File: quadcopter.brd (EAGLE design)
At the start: 137.2 x 137.2 mm, 66 parts, among them J4 AVR_SPI_PRG_6NS, U2 ATMEGA128RFA1

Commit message: CompilingGerber
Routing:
- net VBAT: track 310.7 -> 311.9 mm
- net GND: track 337.0 -> 337.8 mm
- net PE3: track 86.5 -> 87.2 mm
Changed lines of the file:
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@@
 <layer number="13" name="Route13" color="4" fill="5" visible="no" active="no"/>
 <layer number="14" name="Route14" color="1" fill="6" visible="no" active="no"/>
-<layer number="15" name="Route15" color="4" fill="6" visible="no" active="yes"/>
+<layer number="15" name="Route15" color="4" fill="6" visible="yes" active="yes"/>
 <layer number="16" name="Bottom" color="1" fill="1" visible="yes" active="yes"/>
 <layer number="17" name="Pads" color="2" fill="1" visible="yes" active="yes"/>
@@
 <layer number="25" name="tNames" color="7" fill="1" visible="yes" active="yes"/>
 <layer number="26" name="bNames" color="7" fill="1" visible="yes" active="yes"/>
-<layer number="27" name="tValues" color="7" fill="1" visible="yes" active="yes"/>
+<layer number="27" name="tValues" color="7" fill="1" visible="no" active="yes"/>
 <layer number="28" name="bValues" color="7" fill="1" visible="yes" active="yes"/>
-<layer number="29" name="tStop" color="7" fill="3" visible="no" active="yes"/>
+<layer number="29" name="tStop" color="7" fill="3" visible="yes" active="yes"/>
 <layer number="30" name="bStop" color="7" fill="6" visible="no" active="yes"/>
 <layer number="31" name="tCream" color="7" fill="4" visible="no" active="yes"/>
@@
 <layer number="49" name="Reference" color="7" fill="1" visible="yes" active="yes"/>
 <layer number="50" name="dxf" color="7" fill="1" visible="no" active="no"/>
-<layer number="51" name="tDocu" color="7" fill="1" visible="yes" active="yes"/>
+<layer number="51" name="tDocu" color="7" fill="1" visible="no" active="yes"/>
 <layer number="52" name="bDocu" color="7" fill="1" visible="yes" active="yes"/>
 <layer number="53" name="tGND_GNDA" color="7" fill="9" visible="no" active="no"/>
@@
 <wire x1="-28.6385" y1="-38.9255" x2="-38.354" y2="-38.9255" width="0.1524" layer="42"/>
 <wire x1="-38.354" y1="-38.9255" x2="-38.354" y2="-24.7015" width="0.1524" layer="42"/>
+<dimension x1="-5.08" y1="68.58" x2="-5.08" y2="-68.58" x3="-73.4695" y3="0" textsize="1.778" layer="48" unit="inch"/>
 </plain>
 <attributes>
@@
 <wire x1="1.9812" y1="-26.4414" x2="1.96" y2="-26.4355" width="0.1524" layer="1"/>
 <wire x1="-0.1524" y1="-27.432" x2="1.905" y2="-27.432" width="0.1524" layer="1"/>
-<wire x1="-1.3716" y1="-26.2128" x2="-0.1524" y2="-27.432" width="0.1524" layer="1"/>
-<wire x1="-1.9812" y1="-26.2128" x2="-1.3716" y2="-26.2128" width="0.1524" layer="1"/>
-<wire x1="-3.2766" y1="-27.5082" x2="-1.9812" y2="-26.2128" width="0.1524" layer="1"/>
+<wire x1="-1.3716" y1="-26.0223" x2="-0.1524" y2="-27.432" width="0.1524" layer="1"/>
+<wire x1="-1.9812" y1="-26.0223" x2="-1.3716" y2="-26.0223" width="0.1524" layer="1"/>
+<wire x1="-3.2766" y1="-27.5082" x2="-1.9812" y2="-26.0223" width="0.1524" layer="1"/>
 <wire x1="1.905" y1="-27.432" x2="1.96" y2="-27.4355" width="0.1524" layer="1"/>
 <wire x1="-3.2766" y1="-27.5082" x2="-3.302" y2="-27.559" width="0.1524" layer="1"/>
-<wire x1="-9.0678" y1="-31.4706" x2="-10.4394" y2="-32.8422" width="0" layer="19" extent="1-16"/>
 <wire x1="-20.8026" y1="-32.8422" x2="-20.828" y2="-32.899" width="0.1524" layer="1"/>
 <wire x1="-9.0678" y1="-31.4706" x2="-9.023" y2="-31.4325" width="0.1524" layer="1"/>
@@
 <wire x1="-7.6962" y1="-24.4602" x2="-7.802" y2="-24.4355" width="0.1524" layer="1"/>
 <wire x1="-6.7818" y1="-22.7838" x2="-6.8199" y2="-22.7457" width="0.1524" layer="1"/>
-<wire x1="-5.1054" y1="-20.3454" x2="-2.5146" y2="-20.3454" width="0.1524" layer="16"/>
-<wire x1="-5.1816" y1="-20.3454" x2="-5.1054" y2="-20.3454" width="0.1524" layer="1"/>
+<wire x1="-4.1529" y1="-21.1709" x2="-2.5146" y2="-20.3454" width="0.1524" layer="16"/>
+<wire x1="-5.1816" y1="-20.3454" x2="-4.1529" y2="-21.1709" width="0.1524" layer="1"/>
 <wire x1="18.5166" y1="23.0886" x2="19.3548" y2="23.0886" width="0.1524" layer="1"/>
 <wire x1="1.4478" y1="6.0198" x2="18.5166" y2="23.0886" width="0.1524" layer="1"/>
@@
 <via x="-0.9144" y="-21.1074" extent="1-16" drill="0.381"/>
 <via x="-2.5146" y="-20.3454" extent="1-16" drill="0.381"/>
-<via x="-5.1054" y="-20.3454" extent="1-16" drill="0.381"/>
+<via x="-4.1529" y="-21.1709" extent="1-16" drill="0.381"/>
 <via x="-4.6482" y="8.382" extent="1-16" drill="0.381"/>
 <via x="-21.209" y="-25.7175" extent="1-16" drill="0.6"/>
@@
 <wire x1="2.2098" y1="-38.9382" x2="2.2098" y2="-43.1292" width="0.1524" layer="1"/>
 <wire x1="2.2098" y1="-19.5072" x2="2.2098" y2="-38.9382" width="0.1524" layer="16"/>
-<wire x1="1.7526" y1="-19.05" x2="2.2098" y2="-19.5072" width="0.1524" layer="16"/>
-<wire x1="1.0668" y1="-19.05" x2="1.7526" y2="-19.05" width="0.1524" layer="1"/>
+<wire x1="2.3241" y1="-18.542" x2="2.2098" y2="-19.5072" width="0.1524" layer="16"/>
+<wire x1="1.0668" y1="-19.05" x2="2.3241" y2="-18.542" width="0.1524" layer="1"/>
 <wire x1="0.8382" y1="-18.8214" x2="1.0668" y2="-19.05" width="0.1524" layer="1"/>
 <wire x1="2.2098" y1="-43.1292" x2="2.2225" y2="-43.1775" width="0.1524" layer="1"/>
@@
 <wire x1="0.9144" y1="-16.4592" x2="0.2286" y2="-16.4592" width="0.1524" layer="16"/>
 <wire x1="1.7526" y1="-17.2974" x2="0.9144" y2="-16.4592" width="0.1524" layer="16"/>
-<wire x1="1.7526" y1="-19.05" x2="1.7526" y2="-17.2974" width="0.1524" layer="16"/>
+<wire x1="2.3241" y1="-18.542" x2="1.7526" y2="-17.2974" width="0.1524" layer="16"/>
 <via x="2.2098" y="-38.9382" extent="1-16" drill="0.381"/>
-<via x="1.7526" y="-19.05" extent="1-16" drill="0.381"/>
+<via x="2.3241" y="-18.542" extent="1-16" drill="0.381"/>
 </signal>
 <signal name="PE2">
@@
 <wire x1="-5.715" y1="-0.3051" x2="-5.715" y2="-1.5265" width="0.1524" layer="1"/>
 <wire x1="-2.1336" y1="-27.5082" x2="-2.1336" y2="-28.4988" width="0.1524" layer="1"/>
-<wire x1="-1.6764" y1="-27.051" x2="-2.1336" y2="-27.5082" width="0.1524" layer="1"/>
-<wire x1="-1.6764" y1="-24.9174" x2="-1.6764" y2="-27.051" width="0.1524" layer="16"/>
+<wire x1="-1.6764" y1="-26.924" x2="-2.1336" y2="-27.5082" width="0.1524" layer="1"/>
+<wire x1="-1.6764" y1="-24.9174" x2="-1.6764" y2="-26.924" width="0.1524" layer="16"/>
 <wire x1="-7.62" y1="-18.9738" x2="-1.6764" y2="-24.9174" width="0.1524" layer="16"/>
 <wire x1="-7.62" y1="-4.3434" x2="-7.62" y2="-18.9738" width="0.1524" layer="16"/>
@@
 <wire x1="-34.29" y1="13.9446" x2="-34.29" y2="13.97" width="0.1524" layer="16"/>
 <wire x1="-7.62" y1="-4.3434" x2="-7.62" y2="-4.191" width="0.1524" layer="16"/>
-<via x="-1.6764" y="-27.051" extent="1-16" drill="0.381"/>
+<via x="-1.6764" y="-26.924" extent="1-16" drill="0.381"/>
 <via x="-7.62" y="-4.191" extent="1-16" drill="0.381"/>
 </signal>
@@
 <wire x1="-5.715" y1="1.0721" x2="-5.715" y2="1.9025" width="0.1524" layer="1"/>
 <wire x1="-2.7432" y1="-30.2514" x2="-2.7432" y2="-28.575" width="0.1524" layer="1"/>
-<wire x1="-6.1722" y1="-33.6804" x2="-3.946525" y2="-31.454725" width="0" layer="19" extent="1-16"/>
 <wire x1="-3.946525" y1="-31.454725" x2="-2.7432" y2="-30.2514" width="0.1524" layer="1"/>
 <wire x1="-33.4518" y1="10.5918" x2="-33.4518" y2="1.905" width="0.1524" layer="1"/>
@@
 <wire x1="4.4958" y1="-38.7858" x2="4.4958" y2="-36.957" width="0.4572" layer="16"/>
 <wire x1="3.2004" y1="-40.0812" x2="4.4958" y2="-38.7858" width="0.4572" layer="16"/>
-<wire x1="3.2004" y1="-47.1678" x2="3.2004" y2="-40.0812" width="0.4572" layer="16"/>
-<wire x1="2.3622" y1="-48.006" x2="3.2004" y2="-47.1678" width="0.4572" layer="1"/>
+<wire x1="3.8354" y1="-48.0568" x2="3.2004" y2="-40.0812" width="0.4572" layer="16"/>
+<wire x1="2.3622" y1="-48.006" x2="3.8354" y2="-48.0568" width="0.4572" layer="1"/>
 <wire x1="2.8194" y1="-35.2806" x2="2.8025" y2="-35.2425" width="0.4572" layer="1"/>
 <wire x1="2.3622" y1="-48.006" x2="2.2225" y2="-48.1825" width="0.4572" layer="1"/>
@@
 <via x="-3.1242" y="30.48" extent="1-16" drill="0.381"/>
 <via x="4.4958" y="-36.957" extent="1-16" drill="0.381"/>
-<via x="3.2004" y="-47.1678" extent="1-16" drill="0.381"/>
+<via x="3.8354" y="-48.0568" extent="1-16" drill="0.381"/>
 <via x="-39.5478" y="-3.5052" extent="1-16" drill="0.381"/>
 <via x="-37.5666" y="-3.5052" extent="1-16" drill="0.381"/>

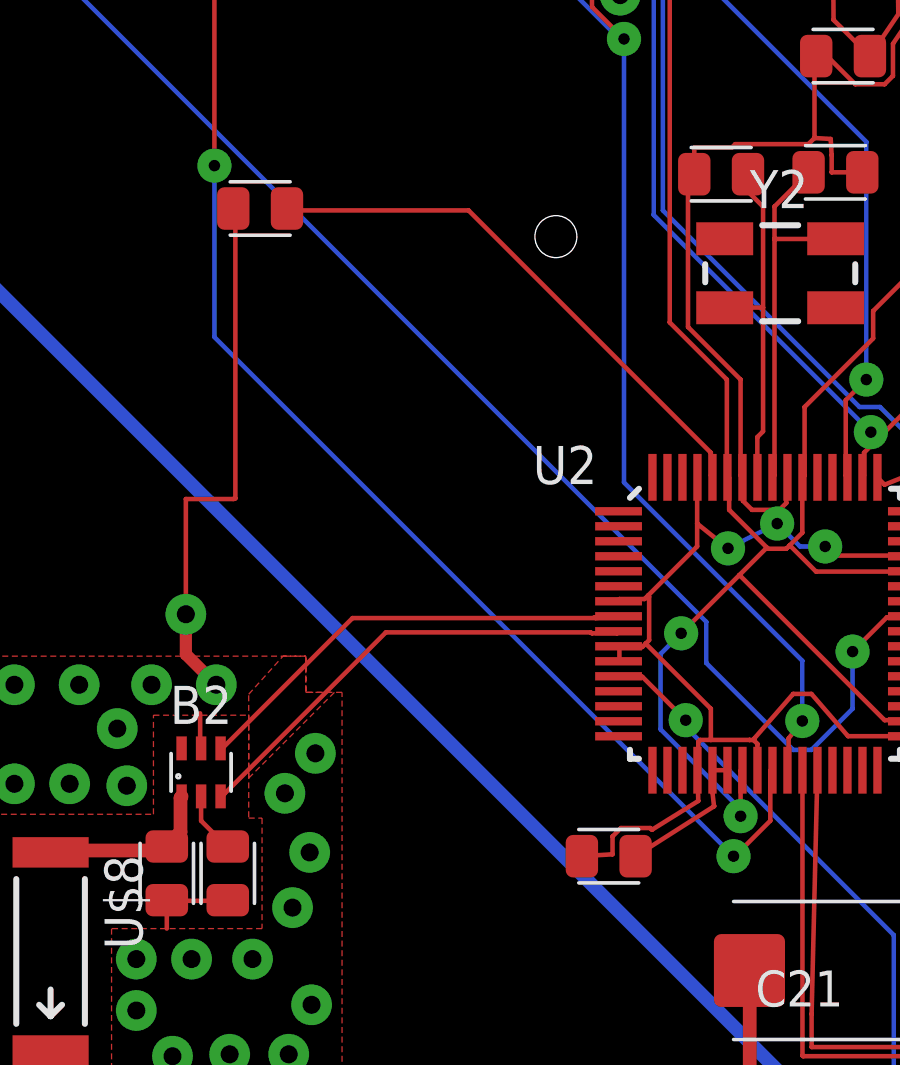
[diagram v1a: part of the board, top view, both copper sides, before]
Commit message: Move Caps closer to microcontroller
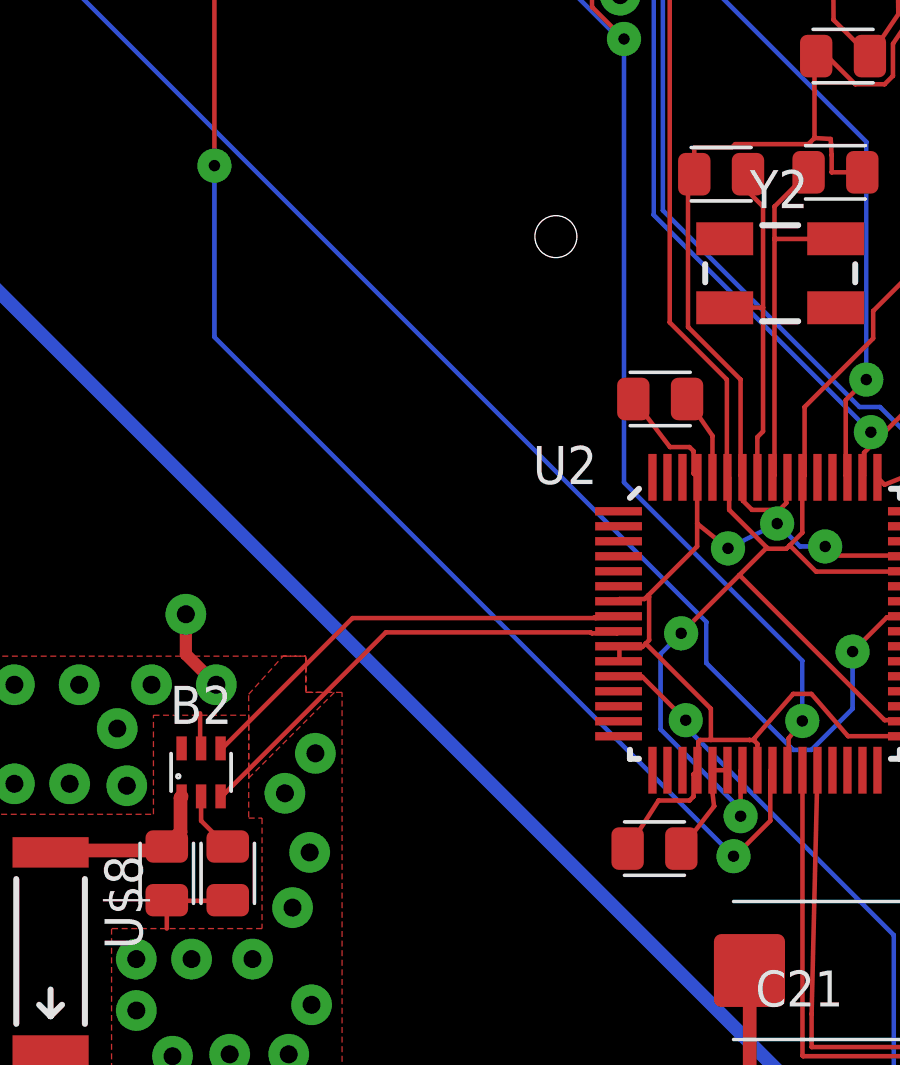
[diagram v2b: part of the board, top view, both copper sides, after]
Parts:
- moved C14 14.8 mm to (-6.41, -16.2)
- moved C15 1.55 mm to (-6.60, -31.2)
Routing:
- net AVDD: track 18.4 -> 2.88 mm
- net GND: track 337.8 -> 324.4 mm
- net DVDD: track 4.81 -> 3.49 mm
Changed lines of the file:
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@@
 <wire x1="-38.354" y1="-38.9255" x2="-38.354" y2="-24.7015" width="0.1524" layer="42"/>
 <dimension x1="-5.08" y1="68.58" x2="-5.08" y2="-68.58" x3="-73.4695" y3="0" textsize="1.778" layer="48" unit="inch"/>
+<dimension x1="-68.58" y1="-5.08" x2="68.58" y2="-5.08" x3="0" y3="-80.645" textsize="1.778" layer="48" unit="inch"/>
 </plain>
 <attributes>
@@
 <attribute name="MPN" value="RC0805JR-0710KL" x="36.3855" y="18.9865" size="1.778" layer="27" rot="R180" display="off"/>
 </element>
-<element name="C14" library="quadparts_prebuilt" package="CAPC2012X140_HS" value="12pF" x="-19.7485" y="-9.8425" rot="R180">
-<attribute name="DIST" value="Digikey" x="-19.7485" y="-9.8425" size="1.778" layer="27" rot="R180" display="off"/>
-<attribute name="DISTPN" value="490-5531-1-ND" x="-19.7485" y="-9.8425" size="1.778" layer="27" rot="R180" display="off"/>
-<attribute name="MFR" value="Murata Electronics North America" x="-19.7485" y="-9.8425" size="1.778" layer="27" rot="R180" display="off"/>
-<attribute name="MPN" value="GRM21A5C2E120JW01D" x="-19.7485" y="-9.8425" size="1.778" layer="27" rot="R180" display="off"/>
-</element>
-<element name="C15" library="quadparts_prebuilt" package="CAPC2012X140_HS" value="12pF" x="-8.128" y="-31.4325" rot="R180">
-<attribute name="DIST" value="Digikey" x="-8.128" y="-31.4325" size="1.778" layer="27" rot="R180" display="off"/>
-<attribute name="DISTPN" value="490-5531-1-ND" x="-8.128" y="-31.4325" size="1.778" layer="27" rot="R180" display="off"/>
-<attribute name="MFR" value="Murata Electronics North America" x="-8.128" y="-31.4325" size="1.778" layer="27" rot="R180" display="off"/>
-<attribute name="MPN" value="GRM21A5C2E120JW01D" x="-8.128" y="-31.4325" size="1.778" layer="27" rot="R180" display="off"/>
+<element name="C14" library="quadparts_prebuilt" package="CAPC2012X140_HS" value="12pF" x="-6.4135" y="-16.1925" rot="R180">
+<attribute name="DIST" value="Digikey" x="-6.4135" y="-16.1925" size="1.778" layer="27" rot="R180" display="off"/>
+<attribute name="DISTPN" value="490-5531-1-ND" x="-6.4135" y="-16.1925" size="1.778" layer="27" rot="R180" display="off"/>
+<attribute name="MFR" value="Murata Electronics North America" x="-6.4135" y="-16.1925" size="1.778" layer="27" rot="R180" display="off"/>
+<attribute name="MPN" value="GRM21A5C2E120JW01D" x="-6.4135" y="-16.1925" size="1.778" layer="27" rot="R180" display="off"/>
+</element>
+<element name="C15" library="quadparts_prebuilt" package="CAPC2012X140_HS" value="12pF" x="-6.604" y="-31.1785" rot="R180">
+<attribute name="DIST" value="Digikey" x="-6.604" y="-31.1785" size="1.778" layer="27" rot="R180" display="off"/>
+<attribute name="DISTPN" value="490-5531-1-ND" x="-6.604" y="-31.1785" size="1.778" layer="27" rot="R180" display="off"/>
+<attribute name="MFR" value="Murata Electronics North America" x="-6.604" y="-31.1785" size="1.778" layer="27" rot="R180" display="off"/>
+<attribute name="MPN" value="GRM21A5C2E120JW01D" x="-6.604" y="-31.1785" size="1.778" layer="27" rot="R180" display="off"/>
 </element>
 <element name="Y2" library="quadparts_prebuilt" package="CRYSTAL-SMD-5X3" value="" x="-2.413" y="-12.0015">
@@
 <wire x1="38.1" y1="-38.227" x2="38.227" y2="-22.606" width="0.1524" layer="1"/>
 <wire x1="38.227" y1="-22.606" x2="35.56" y2="-22.5425" width="0.1524" layer="1"/>
-<wire x1="-5.171" y1="-28.5665" x2="-5.1435" y2="-29.591" width="0.1524" layer="1"/>
-<wire x1="-5.1435" y1="-29.591" x2="-6.68658125" y2="-30.5511375" width="0.1524" layer="1"/>
-<wire x1="-6.68658125" y1="-30.5511375" x2="-6.74381875" y2="-30.4939" width="0.1524" layer="1"/>
-<wire x1="-6.74381875" y1="-30.4939" x2="-7.72218125" y2="-30.4939" width="0.1524" layer="1"/>
-<wire x1="-7.72218125" y1="-30.4939" x2="-8.0016" y2="-30.77331875" width="0.1524" layer="1"/>
-<wire x1="-8.0016" y1="-30.77331875" x2="-8.0016" y2="-31.369" width="0.1524" layer="1"/>
-<wire x1="-8.0016" y1="-31.369" x2="-9.023" y2="-31.4325" width="0.1524" layer="1"/>
 <wire x1="-5.7785" y1="7.245" x2="-4.6482" y2="7.245" width="0.1524" layer="1"/>
 <wire x1="-4.6482" y1="7.245" x2="-3.683" y2="7.245" width="0.1524" layer="1"/>
@@
 <wire x1="-3.2766" y1="-27.5082" x2="-3.302" y2="-27.559" width="0.1524" layer="1"/>
 <wire x1="-20.8026" y1="-32.8422" x2="-20.828" y2="-32.899" width="0.1524" layer="1"/>
-<wire x1="-9.0678" y1="-31.4706" x2="-9.023" y2="-31.4325" width="0.1524" layer="1"/>
 <wire x1="27.051" y1="-35.5092" x2="27.8892" y2="-35.5092" width="0.1524" layer="1"/>
 <wire x1="18.8214" y1="-27.2796" x2="27.051" y2="-35.5092" width="0.1524" layer="1"/>
@@
 <wire x1="-7.7724" y1="-24.4602" x2="-7.802" y2="-24.4355" width="0.1524" layer="1"/>
 <wire x1="-21.717" y1="-27.5844" x2="-21.717" y2="-27.8385" width="0.1524" layer="1"/>
-<wire x1="-20.574" y1="-19.5072" x2="-20.574" y2="-9.906" width="0.1524" layer="1"/>
-<wire x1="-20.574" y1="-9.906" x2="-20.6435" y2="-9.8425" width="0.1524" layer="1"/>
 <wire x1="-5.1816" y1="-21.1074" x2="-5.1816" y2="-20.3454" width="0.1524" layer="1"/>
 <wire x1="-5.1816" y1="-20.3454" x2="-5.1816" y2="-18.8214" width="0.1524" layer="1"/>
@@
 <wire x1="-6.8199" y1="-22.7457" x2="-5.1816" y2="-21.1074" width="0.1524" layer="1"/>
 <wire x1="-7.7724" y1="-22.86" x2="-6.9342" y2="-22.86" width="0.1524" layer="1"/>
-<wire x1="-5.1816" y1="-18.8214" x2="-5.171" y2="-18.8045" width="0.1524" layer="1"/>
+<wire x1="-5.171" y1="-18.8045" x2="-5.1816" y2="-18.8214" width="0.1524" layer="1"/>
 <wire x1="-7.7724" y1="-22.86" x2="-7.802" y2="-22.9355" width="0.1524" layer="1"/>
 <wire x1="-7.0104" y1="-24.4602" x2="-7.6962" y2="-24.4602" width="0.1524" layer="1"/>
@@
 <wire x1="-21.74875" y1="-27.6225" x2="-21.717" y2="-27.8385" width="0.1524" layer="1"/>
 <wire x1="-22.86" y1="-32.899" x2="-22.86" y2="-33.8455" width="0.1524" layer="1"/>
-<wire x1="-22.225" y1="-19.52625" x2="-22.225" y2="-23.368" width="0.1524" layer="1"/>
-<wire x1="-20.6375" y1="-19.52625" x2="-22.225" y2="-19.52625" width="0.1524" layer="1"/>
-<wire x1="-20.6375" y1="-19.52625" x2="-20.574" y2="-19.5072" width="0.1524" layer="1"/>
 <polygon width="0.1524" layer="2">
 <vertex x="-38.1" y="-24.765"/>
@@
 <vertex x="-38.1" y="-38.9255"/>
 </polygon>
+<wire x1="-5.3024" y1="-29.4421875" x2="-5.4363125" y2="-29.5761" width="0.1524" layer="1"/>
+<wire x1="-6.4681" y1="-29.5761" x2="-7.499" y2="-31.1785" width="0.1524" layer="1"/>
+<wire x1="-5.171" y1="-28.5665" x2="-5.3024" y2="-28.6979" width="0.1524" layer="1"/>
+<wire x1="-5.3024" y1="-28.6979" x2="-5.3024" y2="-29.4421875" width="0.1524" layer="1"/>
+<wire x1="-5.4363125" y1="-29.5761" x2="-6.4681" y2="-29.5761" width="0.1524" layer="1"/>
+<wire x1="-5.4363125" y1="-17.7949" x2="-5.3024" y2="-17.9288125" width="0.1524" layer="1"/>
+<wire x1="-5.3024" y1="-17.9288125" x2="-5.3024" y2="-18.6731" width="0.1524" layer="1"/>
+<wire x1="-5.3024" y1="-18.6731" x2="-5.171" y2="-18.8045" width="0.1524" layer="1"/>
+<wire x1="-7.3085" y1="-16.1925" x2="-6.0871" y2="-17.7949" width="0.1524" layer="1"/>
+<wire x1="-6.0871" y1="-17.7949" x2="-5.4363125" y2="-17.7949" width="0.1524" layer="1"/>
 </signal>
 <signal name="DVDD">
@@
 <wire x1="-4.171" y1="-28.5665" x2="-4.671" y2="-28.5665" width="0.1524" layer="1"/>
 <wire x1="-4.6188125" y1="-29.7666" x2="-4.6146" y2="-29.7666" width="0.1524" layer="1"/>
-<wire x1="-4.6146" y1="-29.7666" x2="-7.233" y2="-31.4325" width="0.1524" layer="1"/>
+<wire x1="-4.6146" y1="-29.7666" x2="-5.709" y2="-31.1785" width="0.1524" layer="1"/>
 <wire x1="-4.671" y1="-28.5665" x2="-4.671" y2="-29.3107875" width="0.1524" layer="1"/>
 <wire x1="-4.671" y1="-29.3107875" x2="-4.6188125" y2="-29.7666" width="0.1524" layer="1"/>
@@
 <contactref element="U2" pad="60"/>
 <contactref element="C14" pad="1"/>
-<wire x1="-12.8016" y1="-9.906" x2="-18.8214" y2="-9.906" width="0.1524" layer="1"/>
-<wire x1="-4.7244" y1="-17.9832" x2="-12.8016" y2="-9.906" width="0.1524" layer="1"/>
-<wire x1="-4.7244" y1="-18.7452" x2="-4.7244" y2="-17.9832" width="0.1524" layer="1"/>
-<wire x1="-18.8214" y1="-9.906" x2="-18.8535" y2="-9.8425" width="0.1524" layer="1"/>
-<wire x1="-4.7244" y1="-18.7452" x2="-4.671" y2="-18.8045" width="0.1524" layer="1"/>
+<wire x1="-4.671" y1="-18.8045" x2="-4.671" y2="-17.421" width="0.1524" layer="1"/>
+<wire x1="-4.671" y1="-17.421" x2="-5.5185" y2="-16.1925" width="0.1524" layer="1"/>
 </signal>
 <signal name="RFANT" class="1">
